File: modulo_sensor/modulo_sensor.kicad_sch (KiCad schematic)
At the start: 33 parts, among them J1 Conn_01x08_Pin, U1 74HC14DR2G

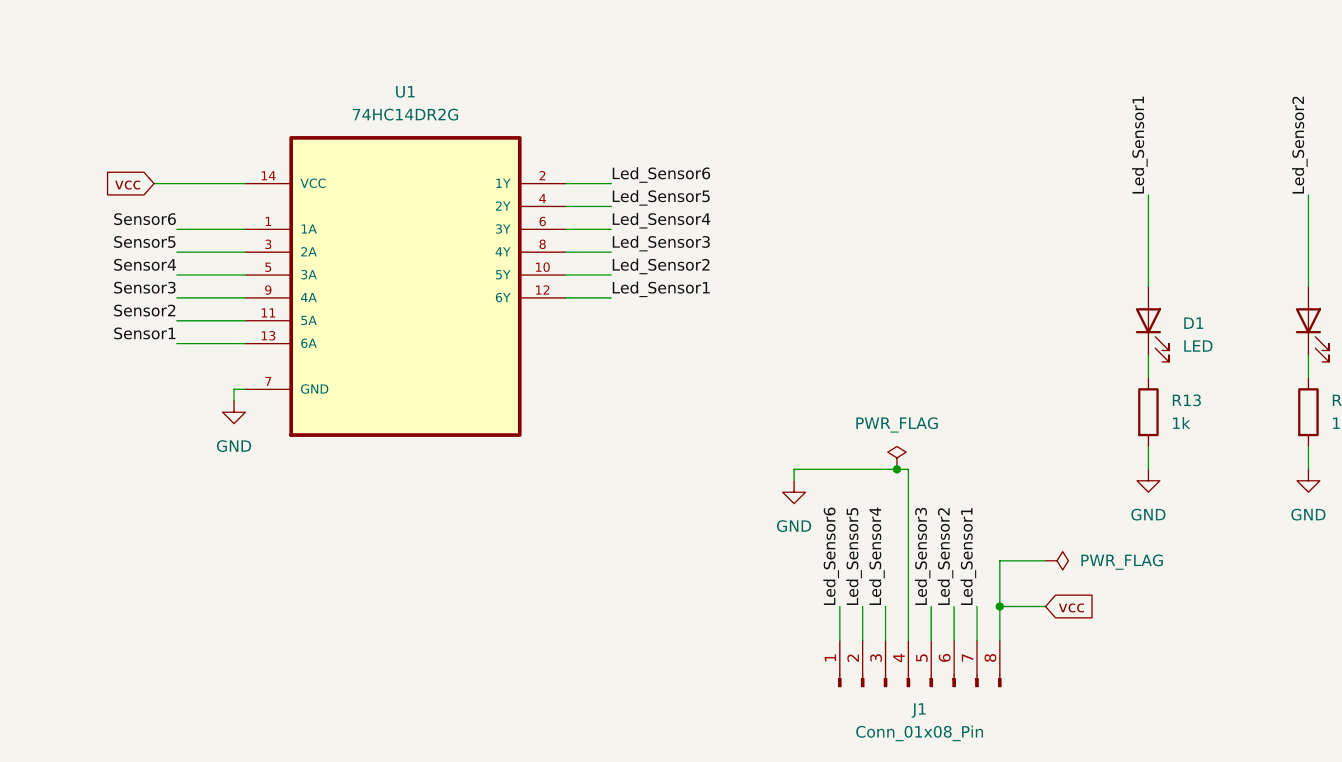
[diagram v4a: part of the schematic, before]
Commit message: feat: Reestructuro la placa a doble faz y pasa el DRC sin errores
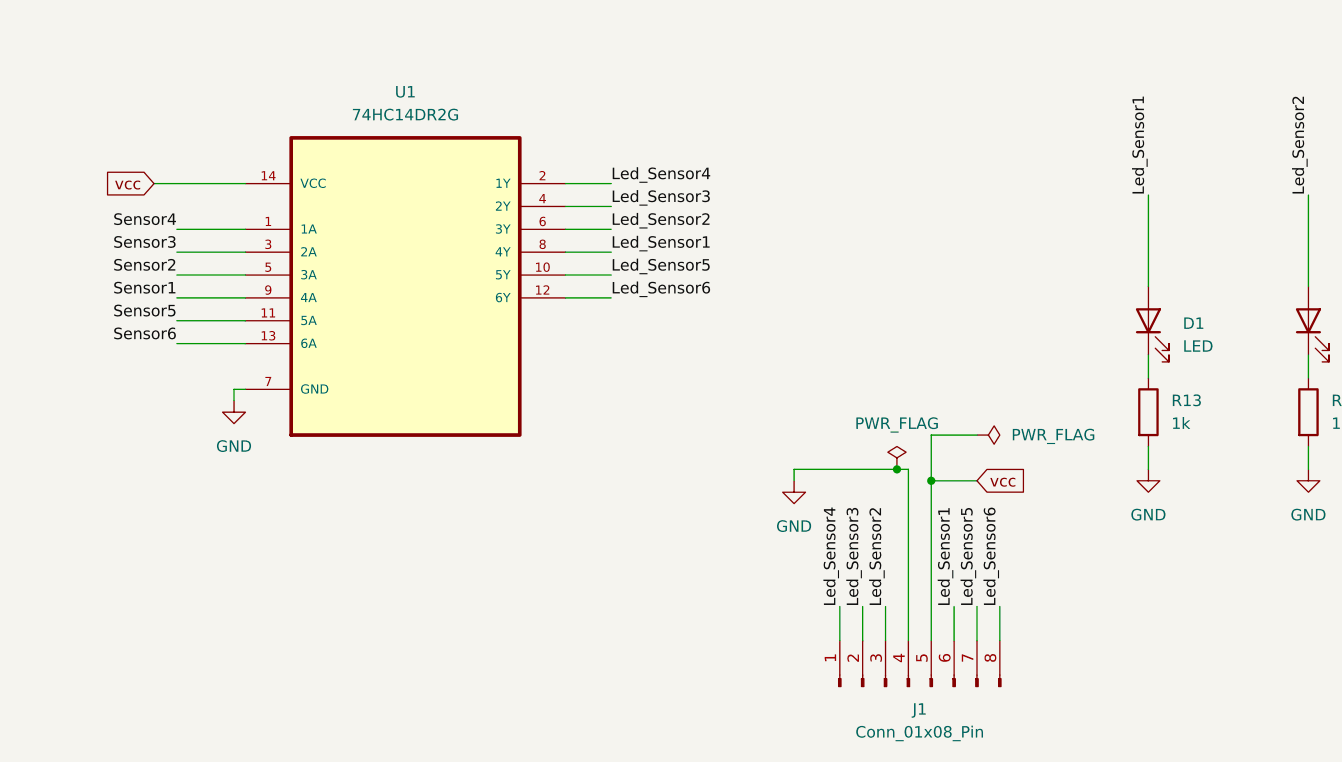
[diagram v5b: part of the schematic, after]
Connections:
- net Led_Sensor1: now also J1.6 (Pin_6), U1.8 (4Y); no longer J1.7 (Pin_7), U1.12 (6Y)
- net Led_Sensor2: now also J1.3 (Pin_3), U1.6 (3Y); no longer J1.6 (Pin_6), U1.10 (5Y)
- net Led_Sensor3: now also J1.2 (Pin_2), U1.4 (2Y); no longer J1.5 (Pin_5), U1.8 (4Y)
- net Led_Sensor4: now also J1.1 (Pin_1), U1.2 (1Y); no longer J1.3 (Pin_3), U1.6 (3Y)
- net Led_Sensor5: now also J1.7 (Pin_7), U1.10 (5Y); no longer J1.2 (Pin_2), U1.4 (2Y)
- net Led_Sensor6: now also J1.8 (Pin_8), U1.12 (6Y); no longer J1.1 (Pin_1), U1.2 (1Y)
- net Sensor1: now also U1.9 (4A); no longer U1.13 (6A)
- net Sensor2: now also U1.5 (3A); no longer U1.11 (5A)
- net Sensor3: now also U1.3 (2A); no longer U1.9 (4A)
- net Sensor4: now also U1.1 (1A); no longer U1.5 (3A)
- net Sensor5: now also U1.11 (5A); no longer U1.3 (2A)
- net Sensor6: now also U1.13 (6A); no longer U1.1 (1A)
- net vcc: now also J1.5 (Pin_5); no longer J1.8 (Pin_8)
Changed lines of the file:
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@@
 	)
 	(junction
-		(at 170.18 64.77)
+		(at 118.11 138.43)
 		(diameter 0)
 		(color 0 0 0 0)
 	)
 	(junction
-		(at 224.79 43.18)
+		(at 170.18 64.77)
 		(diameter 0)
 		(color 0 0 0 0)
 	)
 	(junction
-		(at 125.73 152.4)
+		(at 224.79 43.18)
 		(diameter 0)
 		(color 0 0 0 0)
@@
 	(wire
 		(pts
-			(xy 125.73 152.4) (xy 125.73 156.21)
+			(xy 45.72 43.18) (xy 48.26 43.18)
 		)
 		(stroke
@@
 	(wire
 		(pts
-			(xy 45.72 43.18) (xy 48.26 43.18)
+			(xy 207.01 46.99) (xy 195.58 46.99)
 		)
 		(stroke
@@
 	(wire
 		(pts
-			(xy 207.01 46.99) (xy 195.58 46.99)
+			(xy 77.47 118.11) (xy 82.55 118.11)
 		)
 		(stroke
@@
 	(wire
 		(pts
-			(xy 77.47 118.11) (xy 82.55 118.11)
+			(xy 125.73 152.4) (xy 125.73 156.21)
 		)
 		(stroke
@@
 	(wire
 		(pts
+			(xy 118.11 138.43) (xy 118.11 156.21)
+		)
+		(stroke
+			(width 0)
+			(type default)
+		)
+	)
+	(wire
+		(pts
 			(xy 34.29 110.49) (xy 41.91 110.49)
 		)
@@
 	(wire
 		(pts
-			(xy 125.73 152.4) (xy 130.81 152.4)
+			(xy 118.11 138.43) (xy 123.19 138.43)
 		)
 		(stroke
@@
 	(wire
 		(pts
-			(xy 125.73 147.32) (xy 125.73 152.4)
+			(xy 118.11 133.35) (xy 118.11 138.43)
 		)
 		(stroke
@@
 	(wire
 		(pts
-			(xy 118.11 152.4) (xy 118.11 156.21)
-		)
-		(stroke
-			(width 0)
-			(type default)
-		)
-	)
-	(wire
-		(pts
 			(xy 170.18 43.18) (xy 172.72 43.18)
 		)
@@
 	(wire
 		(pts
-			(xy 130.81 147.32) (xy 125.73 147.32)
+			(xy 123.19 133.35) (xy 118.11 133.35)
 		)
 		(stroke
@@
 		)
 	)
-	(label "Led_Sensor1"
-		(at 123.19 152.4 90)
+	(label "Led_Sensor4"
+		(at 107.95 152.4 90)
 		(fields_autoplaced yes)
 		(effects
@@
 		)
 	)
-	(label "Led_Sensor1"
+	(label "Led_Sensor6"
 		(at 82.55 118.11 0)
 		(fields_autoplaced yes)
@@
 		)
 	)
-	(label "Led_Sensor3"
+	(label "Led_Sensor1"
 		(at 82.55 113.03 0)
 		(fields_autoplaced yes)
@@
 		)
 	)
-	(label "Led_Sensor6"
+	(label "Led_Sensor4"
 		(at 82.55 105.41 0)
 		(fields_autoplaced yes)
@@
 		)
 	)
-	(label "Sensor3"
+	(label "Sensor1"
 		(at 34.29 118.11 180)
 		(fields_autoplaced yes)
@@
 		)
 	)
-	(label "Sensor6"
+	(label "Sensor4"
 		(at 34.29 110.49 180)
 		(fields_autoplaced yes)
@@
 		)
 	)
-	(label "Led_Sensor3"
-		(at 118.11 152.4 90)
+	(label "Led_Sensor2"
+		(at 113.03 152.4 90)
 		(fields_autoplaced yes)
 		(effects
@@
 		)
 	)
-	(label "Sensor1"
+	(label "Sensor6"
 		(at 34.29 123.19 180)
 		(fields_autoplaced yes)
@@
 		)
 	)
-	(label "Sensor4"
+	(label "Sensor2"
 		(at 34.29 115.57 180)
 		(fields_autoplaced yes)
@@
 	)
 	(label "Led_Sensor5"
-		(at 110.49 152.4 90)
+		(at 123.19 152.4 90)
 		(fields_autoplaced yes)
 		(effects
@@
 		)
 	)
-	(label "Led_Sensor2"
-		(at 120.65 152.4 90)
+	(label "Led_Sensor3"
+		(at 110.49 152.4 90)
 		(fields_autoplaced yes)
 		(effects
@@
 		)
 	)
-	(label "Led_Sensor4"
+	(label "Led_Sensor2"
 		(at 82.55 110.49 0)
 		(fields_autoplaced yes)
@@
 	)
 	(label "Led_Sensor6"
-		(at 107.95 152.4 90)
+		(at 125.73 152.4 90)
 		(fields_autoplaced yes)
 		(effects
@@
 		)
 	)
-	(label "Led_Sensor4"
-		(at 113.03 152.4 90)
+	(label "Led_Sensor1"
+		(at 120.65 152.4 90)
 		(fields_autoplaced yes)
 		(effects
@@
 		)
 	)
-	(label "Sensor5"
+	(label "Sensor3"
 		(at 34.29 113.03 180)
 		(fields_autoplaced yes)
@@
 		)
 	)
-	(label "Led_Sensor5"
+	(label "Led_Sensor3"
 		(at 82.55 107.95 0)
 		(fields_autoplaced yes)
@@
 		)
 	)
-	(label "Sensor2"
+	(label "Sensor5"
 		(at 34.29 120.65 180)
 		(fields_autoplaced yes)
@@
 		)
 	)
-	(label "Led_Sensor2"
+	(label "Led_Sensor5"
 		(at 82.55 115.57 0)
 		(fields_autoplaced yes)
@@
 	(global_label "vcc"
 		(shape input)
-		(at 130.81 152.4 0)
+		(at 123.19 138.43 0)
 		(fields_autoplaced yes)
 		(effects
@@
 		)
 		(property "Intersheetrefs" "${INTERSHEET_REFS}"
-			(at 136.94 152.4 0)
+			(at 129.32 138.43 0)
 			(effects
 				(font
@@
 	(symbol
 		(lib_id "power:PWR_FLAG")
-		(at 130.81 147.32 270)
+		(at 123.19 133.35 270)
 		(unit 1)
 		(exclude_from_sim no)
@@
 		(dnp no)
 		(property "Reference" "#FLG02"
-			(at 132.715 147.32 0)
+			(at 125.095 133.35 0)
 			(effects
 				(font
@@
 		)
 		(property "Value" "PWR_FLAG"
-			(at 134.62 147.3199 90)
+			(at 127 133.3499 90)
 			(effects
 				(font
@@
 		)
 		(property "Footprint" ""
-			(at 130.81 147.32 0)
+			(at 123.19 133.35 0)
 			(effects
 				(font
@@
 		)
 		(property "Datasheet" "~"
-			(at 130.81 147.32 0)
+			(at 123.19 133.35 0)
 			(effects
 				(font
@@
 		)
 		(property "Description" "Special symbol for telling ERC where power comes from"
-			(at 130.81 147.32 0)
+			(at 123.19 133.35 0)
 			(effects
 				(font

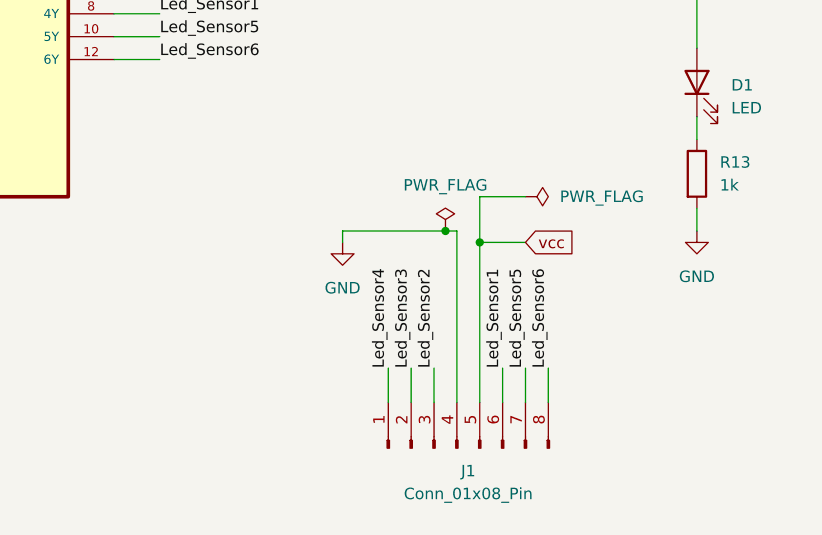
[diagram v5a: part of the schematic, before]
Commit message: refactor: Reodeno los pines para acomodarlos en la pcb
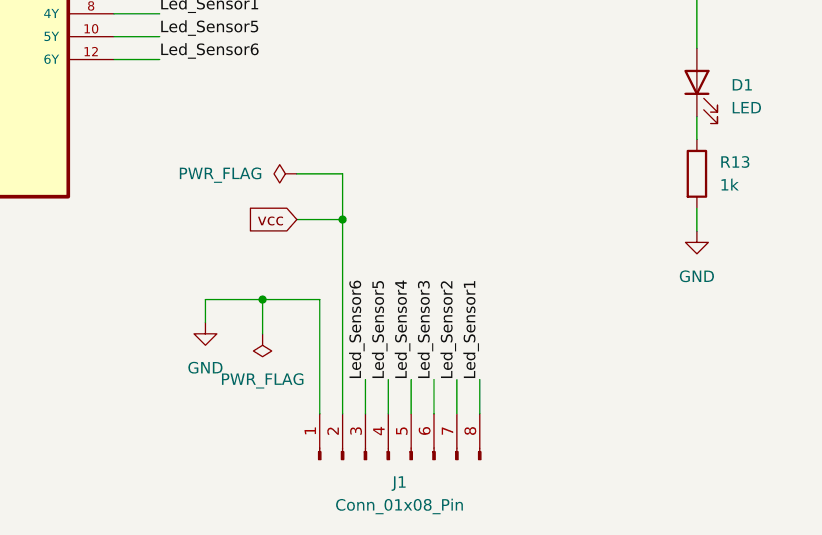
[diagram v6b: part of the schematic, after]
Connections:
- net GND: now also J1.1 (Pin_1); no longer J1.4 (Pin_4)
- net Led_Sensor1: now also J1.8 (Pin_8); no longer J1.6 (Pin_6)
- net Led_Sensor2: now also J1.7 (Pin_7); no longer J1.3 (Pin_3)
- net Led_Sensor3: now also J1.6 (Pin_6); no longer J1.2 (Pin_2)
- net Led_Sensor4: now also J1.5 (Pin_5); no longer J1.1 (Pin_1)
- net Led_Sensor5: now also J1.4 (Pin_4); no longer J1.7 (Pin_7)
- net Led_Sensor6: now also J1.3 (Pin_3); no longer J1.8 (Pin_8)
- net vcc: now also J1.2 (Pin_2); no longer J1.5 (Pin_5)
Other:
- moved on the sheet: J1
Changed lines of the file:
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@@
 	)
 	(junction
-		(at 114.3 137.16)
-		(diameter 0)
-		(color 0 0 0 0)
-	)
-	(junction
 		(at 106.68 62.23)
 		(diameter 0)
@@
 	)
 	(junction
-		(at 118.11 138.43)
+		(at 102.87 135.89)
 		(diameter 0)
 		(color 0 0 0 0)
@@
 	)
 	(junction
+		(at 93.98 144.78)
+		(diameter 0)
+		(color 0 0 0 0)
+	)
+	(junction
 		(at 135.89 43.18)
 		(diameter 0)
@@
 	(wire
 		(pts
-			(xy 102.87 137.16) (xy 102.87 138.43)
+			(xy 95.25 48.26) (xy 92.71 48.26)
 		)
 		(stroke
@@
 	(wire
 		(pts
-			(xy 95.25 48.26) (xy 92.71 48.26)
+			(xy 34.29 113.03) (xy 41.91 113.03)
 		)
 		(stroke
@@
 	(wire
 		(pts
-			(xy 34.29 113.03) (xy 41.91 113.03)
+			(xy 113.03 157.48) (xy 113.03 153.67)
 		)
 		(stroke
@@
 	(wire
 		(pts
-			(xy 123.19 152.4) (xy 123.19 156.21)
+			(xy 102.87 135.89) (xy 102.87 157.48)
 		)
 		(stroke
@@
 	(wire
 		(pts
-			(xy 125.73 152.4) (xy 125.73 156.21)
-		)
-		(stroke
-			(width 0)
-			(type default)
-		)
-	)
-	(wire
-		(pts
-			(xy 120.65 152.4) (xy 120.65 156.21)
-		)
-		(stroke
-			(width 0)
-			(type default)
-		)
-	)
-	(wire
-		(pts
-			(xy 118.11 138.43) (xy 118.11 156.21)
+			(xy 118.11 153.67) (xy 118.11 157.48)
 		)
 		(stroke
@@
 	(wire
 		(pts
-			(xy 118.11 138.43) (xy 123.19 138.43)
+			(xy 102.87 135.89) (xy 97.79 135.89)
 		)
 		(stroke
@@
 	(wire
 		(pts
-			(xy 107.95 152.4) (xy 107.95 156.21)
+			(xy 105.41 153.67) (xy 105.41 157.48)
 		)
 		(stroke
@@
 	(wire
 		(pts
+			(xy 87.63 144.78) (xy 87.63 147.32)
+		)
+		(stroke
+			(width 0)
+			(type default)
+		)
+	)
+	(wire
+		(pts
 			(xy 254 62.23) (xy 254 64.77)
 		)
@@
 	(wire
 		(pts
-			(xy 114.3 137.16) (xy 115.57 137.16)
+			(xy 100.33 144.78) (xy 93.98 144.78)
 		)
 		(stroke
@@
 	(wire
 		(pts
-			(xy 118.11 133.35) (xy 118.11 138.43)
+			(xy 102.87 130.81) (xy 102.87 135.89)
 		)
 		(stroke
@@
 	(wire
 		(pts
-			(xy 113.03 152.4) (xy 113.03 156.21)
+			(xy 110.49 153.67) (xy 110.49 157.48)
 		)
 		(stroke
@@
 	(wire
 		(pts
+			(xy 115.57 157.48) (xy 115.57 153.67)
+		)
+		(stroke
+			(width 0)
+			(type default)
+		)
+	)
+	(wire
+		(pts
 			(xy 224.79 43.18) (xy 227.33 43.18)
 		)
@@
 	(wire
 		(pts
-			(xy 102.87 137.16) (xy 114.3 137.16)
+			(xy 87.63 144.78) (xy 93.98 144.78)
 		)
 		(stroke
@@
 	(wire
 		(pts
-			(xy 123.19 133.35) (xy 118.11 133.35)
+			(xy 97.79 130.81) (xy 102.87 130.81)
 		)
 		(stroke
@@
 	(wire
 		(pts
-			(xy 115.57 137.16) (xy 115.57 156.21)
+			(xy 100.33 144.78) (xy 100.33 157.48)
 		)
 		(stroke
@@
 	(wire
 		(pts
-			(xy 110.49 152.4) (xy 110.49 156.21)
+			(xy 107.95 153.67) (xy 107.95 157.48)
 		)
 		(stroke
@@
 	(wire
 		(pts
+			(xy 93.98 148.59) (xy 93.98 144.78)
+		)
+		(stroke
+			(width 0)
+			(type default)
+		)
+	)
+	(wire
+		(pts
 			(xy 266.7 43.18) (xy 269.24 43.18)
 		)
@@
 		)
 	)
-	(label "Led_Sensor4"
-		(at 107.95 152.4 90)
+	(label "Led_Sensor6"
+		(at 105.41 153.67 90)
 		(fields_autoplaced yes)
 		(effects
@@
 		)
 	)
-	(label "Led_Sensor2"
-		(at 113.03 152.4 90)
+	(label "Led_Sensor4"
+		(at 110.49 153.67 90)
 		(fields_autoplaced yes)
 		(effects
@@
 		)
 	)
-	(label "Led_Sensor5"
-		(at 123.19 152.4 90)
+	(label "Led_Sensor2"
+		(at 115.57 153.67 90)
 		(fields_autoplaced yes)
 		(effects
@@
 		)
 	)
-	(label "Led_Sensor3"
-		(at 110.49 152.4 90)
+	(label "Led_Sensor5"
+		(at 107.95 153.67 90)
 		(fields_autoplaced yes)
 		(effects
@@
 		)
 	)
-	(label "Led_Sensor6"
-		(at 125.73 152.4 90)
+	(label "Led_Sensor1"
+		(at 118.11 153.67 90)
 		(fields_autoplaced yes)
 		(effects
@@
 		)
 	)
-	(label "Led_Sensor1"
-		(at 120.65 152.4 90)
+	(label "Led_Sensor3"
+		(at 113.03 153.67 90)
 		(fields_autoplaced yes)
 		(effects
@@
 	(global_label "vcc"
 		(shape input)
-		(at 123.19 138.43 0)
+		(at 97.79 135.89 180)
 		(fields_autoplaced yes)
 		(effects
@@
 				(size 1.27 1.27)
 			)
-			(justify left)
+			(justify right)
 		)
 		(property "Intersheetrefs" "${INTERSHEET_REFS}"
-			(at 129.32 138.43 0)
+			(at 91.66 135.89 0)
 			(effects
 				(font
 					(size 1.27 1.27)
 				)
-				(justify left)
+				(justify right)
 				(hide yes)
 			)
@@
 	(symbol
 		(lib_id "power:GND")
-		(at 102.87 138.43 0)
+		(at 87.63 147.32 0)
 		(unit 1)
 		(exclude_from_sim no)
@@
 		(dnp no)
 		(property "Reference" "#PWR012"
-			(at 102.87 144.78 0)
+			(at 87.63 153.67 0)
 			(effects
 				(font
@@
 		)
 		(property "Value" "GND"
-			(at 102.87 143.51 0)
+			(at 87.63 152.4 0)
 			(effects
 				(font
@@
 		)
 		(property "Footprint" ""
-			(at 102.87 138.43 0)
+			(at 87.63 147.32 0)
 			(effects
 				(font
@@
 		)
 		(property "Datasheet" ""
-			(at 102.87 138.43 0)
+			(at 87.63 147.32 0)
 			(effects
 				(font
@@
 		)
 		(property "Description" "Power symbol creates a global label with name \"GND\" , ground"
-			(at 102.87 138.43 0)
+			(at 87.63 147.32 0)
 			(effects
 				(font
@@
 	(symbol
 		(lib_id "power:PWR_FLAG")
-		(at 114.3 137.16 0)
+		(at 93.98 148.59 180)
 		(unit 1)
 		(exclude_from_sim no)
@@
 		(dnp no)
 		(property "Reference" "#FLG01"
-			(at 114.3 135.255 0)
+			(at 93.98 150.495 0)
 			(effects
 				(font
@@
 		)
 		(property "Value" "PWR_FLAG"
-			(at 114.3 132.08 0)
+			(at 93.98 153.67 0)
 			(effects
 				(font
@@
 		)
 		(property "Footprint" ""
-			(at 114.3 137.16 0)
+			(at 93.98 148.59 0)
 			(effects
 				(font
@@
 		)
 		(property "Datasheet" "~"
-			(at 114.3 137.16 0)
+			(at 93.98 148.59 0)
 			(effects
 				(font
@@
 		)
 		(property "Description" "Special symbol for telling ERC where power comes from"
-			(at 114.3 137.16 0)
+			(at 93.98 148.59 0)
 			(effects
 				(font
@@
 	(symbol
 		(lib_id "Connector:Conn_01x08_Pin")
-		(at 115.57 161.29 90)
+		(at 107.95 162.56 90)
 		(unit 1)
 		(exclude_from_sim no)
@@
 		(fields_autoplaced yes)
 		(property "Reference" "J1"
-			(at 116.84 163.83 90)
+			(at 109.22 165.1 90)
 			(effects
 				(font
@@
 		)
 		(property "Value" "Conn_01x08_Pin"
-			(at 116.84 166.37 90)
+			(at 109.22 167.64 90)
 			(effects
 				(font
@@
 		)
 		(property "Footprint" "Connector_PinHeader_1.27mm:PinHeader_1x08_P1.27mm_Horizontal"
-			(at 115.57 161.29 0)
+			(at 107.95 162.56 0)
 			(effects
 				(font
@@
 		)
 		(property "Datasheet" "~"
-			(at 115.57 161.29 0)
+			(at 107.95 162.56 0)
 			(effects
 				(font
@@
 		)
 		(property "Description" "Generic connector, single row, 01x08, script generated"
-			(at 115.57 161.29 0)
+			(at 107.95 162.56 0)
 			(effects
 				(font
@@
 	(symbol
 		(lib_id "power:PWR_FLAG")
-		(at 123.19 133.35 270)
+		(at 97.79 130.81 90)
+		(mirror x)
 		(unit 1)
 		(exclude_from_sim no)
@@
 		(dnp no)
 		(property "Reference" "#FLG02"
-			(at 125.095 133.35 0)
+			(at 95.885 130.81 0)
 			(effects
 				(font
@@
 		)
 		(property "Value" "PWR_FLAG"
-			(at 127 133.3499 90)
+			(at 93.98 130.8099 90)
 			(effects
 				(font
@@
 		)
 		(property "Footprint" ""
-			(at 123.19 133.35 0)
+			(at 97.79 130.81 0)
 			(effects
 				(font
@@
 		)
 		(property "Datasheet" "~"
-			(at 123.19 133.35 0)
+			(at 97.79 130.81 0)
 			(effects
 				(font
@@
 		)
 		(property "Description" "Special symbol for telling ERC where power comes from"
-			(at 123.19 133.35 0)
+			(at 97.79 130.81 0)
 			(effects
 				(font

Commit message: refactor(modulo_sensor): Cambio la huella del pin por una de 2,5mm
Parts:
- J1: footprint Connector_PinHeader_1.27mm:PinHeader_1x08_P1.27mm_Horizontal -> Connector_PinHeader_2.54mm:PinHeader_1x08_P2.54mm_Horizontal
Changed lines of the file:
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@@
 			)
 		)
-		(property "Footprint" "Connector_PinHeader_1.27mm:PinHeader_1x08_P1.27mm_Horizontal"
+		(property "Footprint" "Connector_PinHeader_2.54mm:PinHeader_1x08_P2.54mm_Horizontal"
 			(at 107.95 162.56 0)
 			(effects

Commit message: feat(modulo-sensor): Agrego vías y actualizo las previews del circuito
Commit de Cinthia
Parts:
- Sensor1, Sensor2, Sensor3, Sensor4, Sensor5, Sensor6: footprint TCRT5000:OPTO_TCRT5000 -> TCRT5000:OPTO_TCRT5000_ancho
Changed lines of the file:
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@@
 			)
 		)
-		(property "Footprint" "TCRT5000:OPTO_TCRT5000"
+		(property "Footprint" "TCRT5000:OPTO_TCRT5000_ancho"
 			(at 167.64 54.61 0)
 			(effects
@@
 			)
 		)
-		(property "Footprint" "TCRT5000:OPTO_TCRT5000"
+		(property "Footprint" "TCRT5000:OPTO_TCRT5000_ancho"
 			(at 209.55 54.61 0)
 			(effects
@@
 			)
 		)
-		(property "Footprint" "TCRT5000:OPTO_TCRT5000"
+		(property "Footprint" "TCRT5000:OPTO_TCRT5000_ancho"
 			(at 77.47 54.61 0)
 			(effects
@@
 			)
 		)
-		(property "Footprint" "TCRT5000:OPTO_TCRT5000"
+		(property "Footprint" "TCRT5000:OPTO_TCRT5000_ancho"
 			(at 251.46 54.61 0)
 			(effects
@@
 			)
 		)
-		(property "Footprint" "TCRT5000:OPTO_TCRT5000"
+		(property "Footprint" "TCRT5000:OPTO_TCRT5000_ancho"
 			(at 120.65 54.61 0)
 			(effects
@@
 			)
 		)
-		(property "Footprint" "TCRT5000:OPTO_TCRT5000"
+		(property "Footprint" "TCRT5000:OPTO_TCRT5000_ancho"
 			(at 33.02 54.61 0)
 			(effects
